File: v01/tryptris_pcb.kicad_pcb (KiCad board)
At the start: 2 copper layers, 298.8 x 122 mm, 131 parts, among them J1 USB_C_Receptacle_USB2.0, J2 I2C-L, J3 I2C-R, SW1 Reset, U1 ATmega32U4-AU, U2 MCP23017_SO, Y1 16Mhz

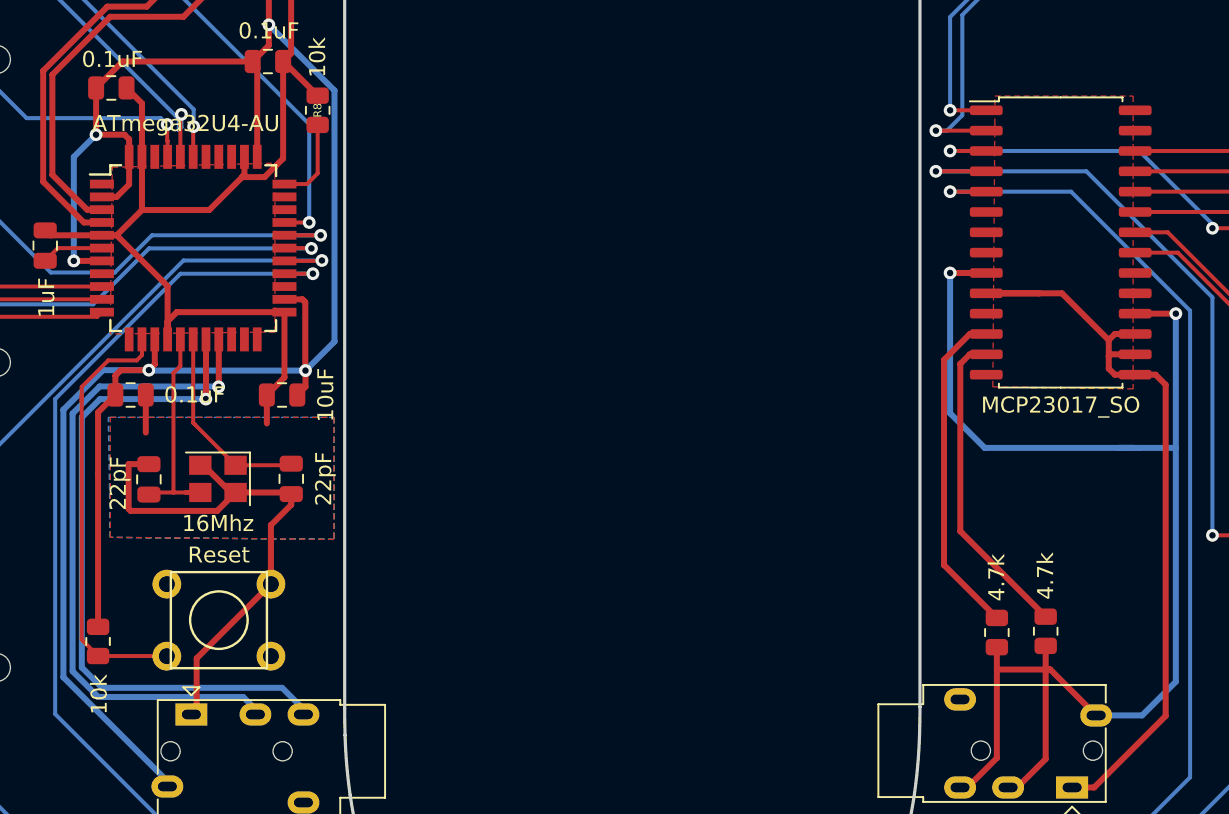
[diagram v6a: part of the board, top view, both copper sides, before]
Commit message: Fix ERC and DRC errors.
Move right half to use VSS instead of GND and add power flags to remove
net links between sides.
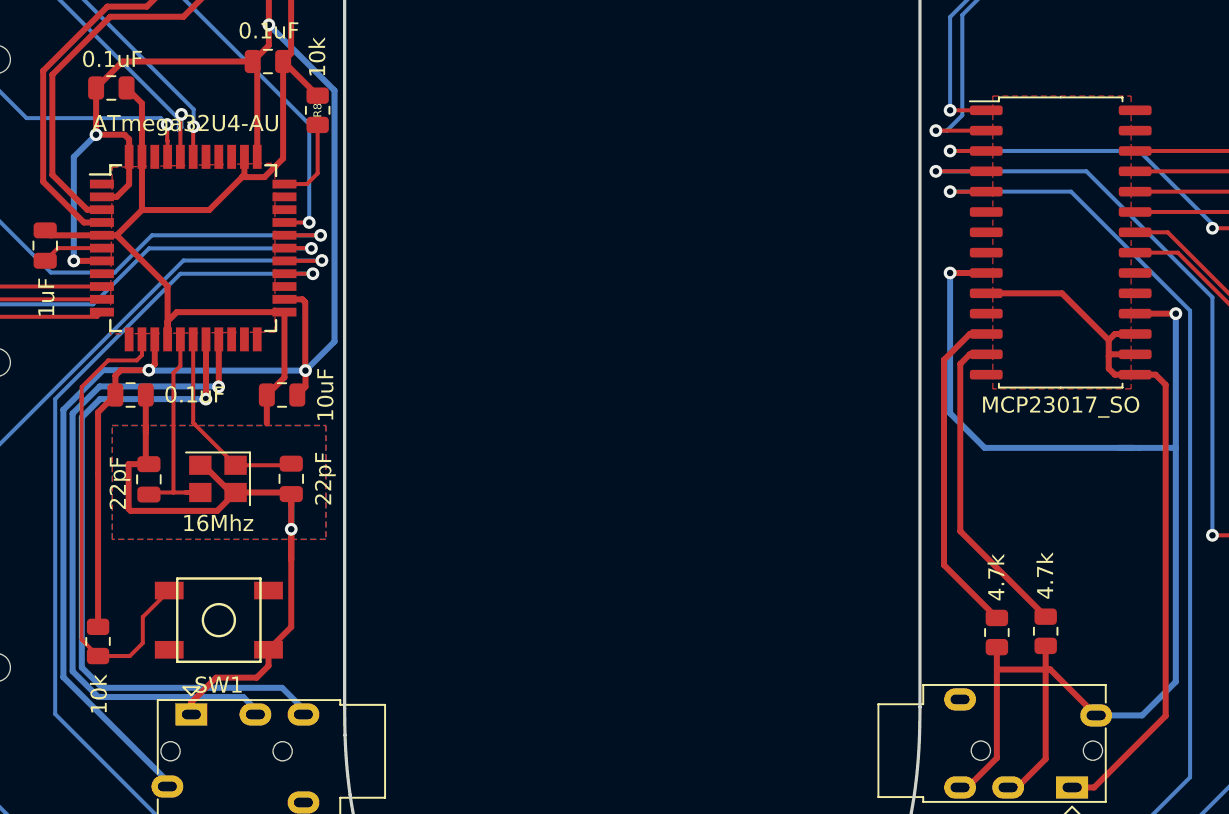
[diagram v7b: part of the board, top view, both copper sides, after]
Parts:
- SW1: footprint random-keyboard-parts:PushButton_6x6mm_TH -> random-keyboard-parts:SKQG-1155865
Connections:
- J3 pad T: GND -> VSS
- U2 pad 10: GND -> VSS
- U2 pad 15: GND -> VSS
- U2 pad 16: GND -> VSS
- U2 pad 17: GND -> VSS
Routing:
- net VSS: track 0.00 -> 46.4 mm
- net GND: track 196.9 -> 153.1 mm, vias 0 -> 1
- net Net-(R1-Pad2): track 27.7 -> 30.3 mm
- added copper zone on F.Cu, net VSS

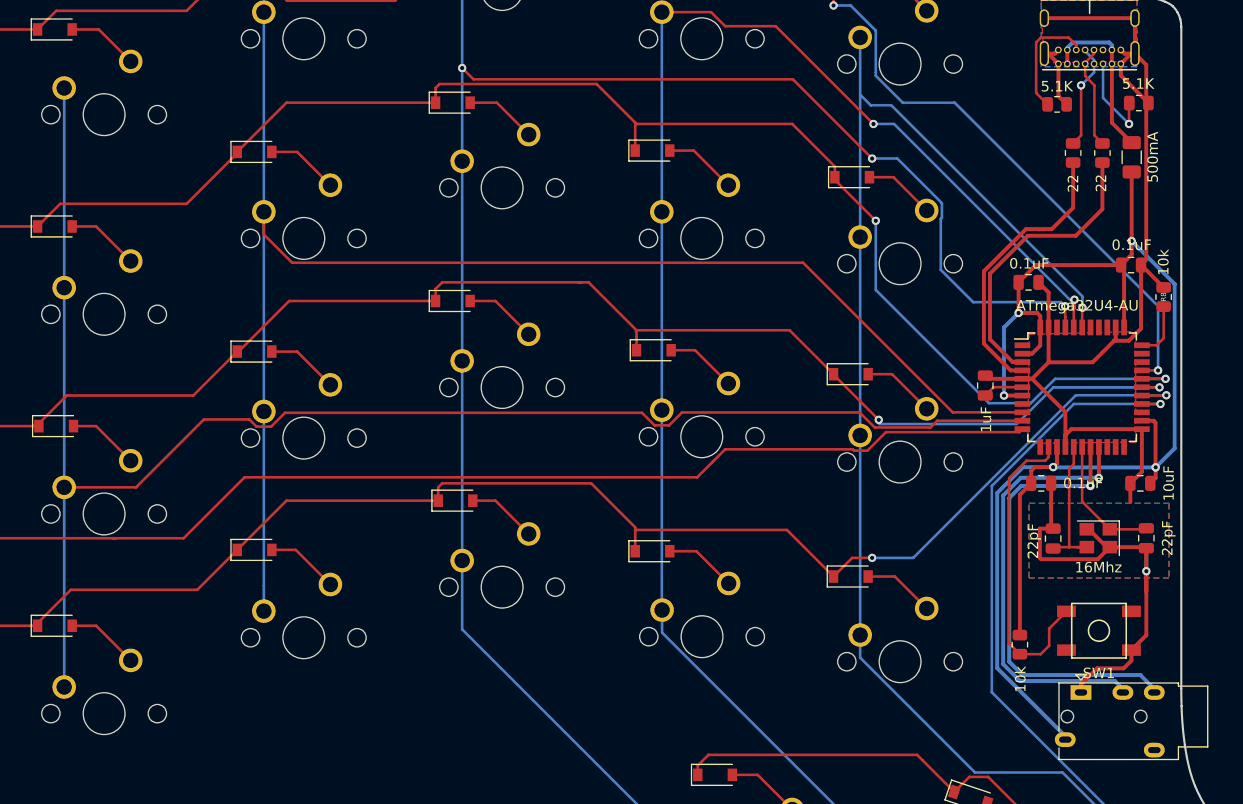
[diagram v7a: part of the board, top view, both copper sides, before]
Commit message: Improve routing around crystal
* I had scl and sda running under the crystal.
* Fix 5v not going through decoupling capacitors.
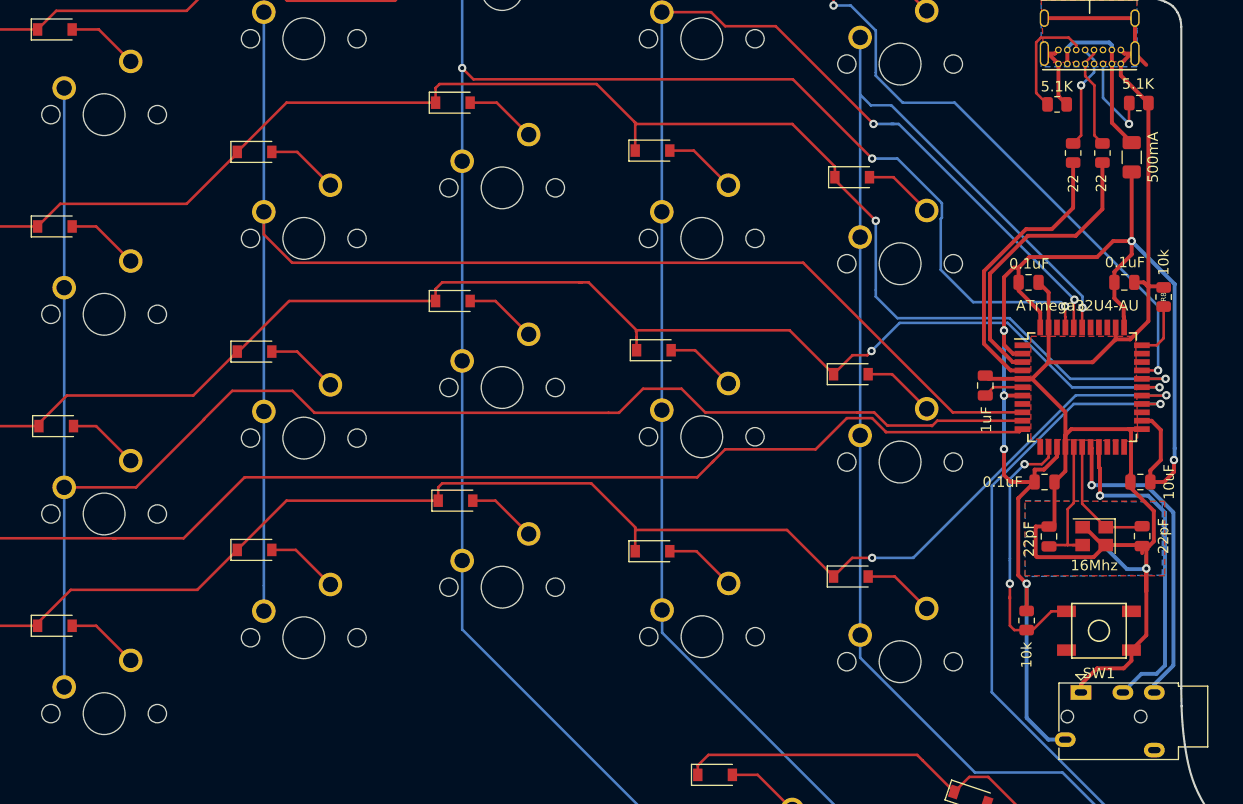
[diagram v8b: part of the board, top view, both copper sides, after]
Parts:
- moved R1 2.39 mm to (143.3, 98.2)
- moved C4 1.77 mm to (152.6, 65.9)
- moved C1 0.45 mm to (154.3, 90.1)
- moved C2 0.45 mm to (145.4, 90.2)
- moved Y1 0.45 mm to (149.7, 90.1)
- moved C5 0.34 mm to (145.0, 85.0)
- moved C7 0.13 mm to (154.1, 85.0)
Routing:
- net SCL-L: track 43.0 -> 30.7 mm
- net SDA-L: track 41.8 -> 31.2 mm
- net GND: track 153.1 -> 163.2 mm
- net +5V: track 141.0 -> 133.4 mm, vias 5 -> 6
- net Net-(R1-Pad2): track 30.3 -> 26.3 mm, vias 0 -> 2
- net Col1: track 154.0 -> 156.1 mm
- net Row1-L: track 158.3 -> 156.7 mm
- net Col4: track 152.0 -> 150.6 mm
- net Col0: track 175.7 -> 176.7 mm
- net Row2-L: track 146.1 -> 147.1 mm
